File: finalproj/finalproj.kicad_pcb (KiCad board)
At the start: 2 copper layers, 35 parts, among them J10 Motor Out B, J11 Motor Out A, J5 Stepper_Motor_Controller, J7 LIDAR_Connector, J9 RPI_UART_Conn, U2 LM1085-12, U3 LM1085-5.0, U4 LM1085-3.3, U5 L298N

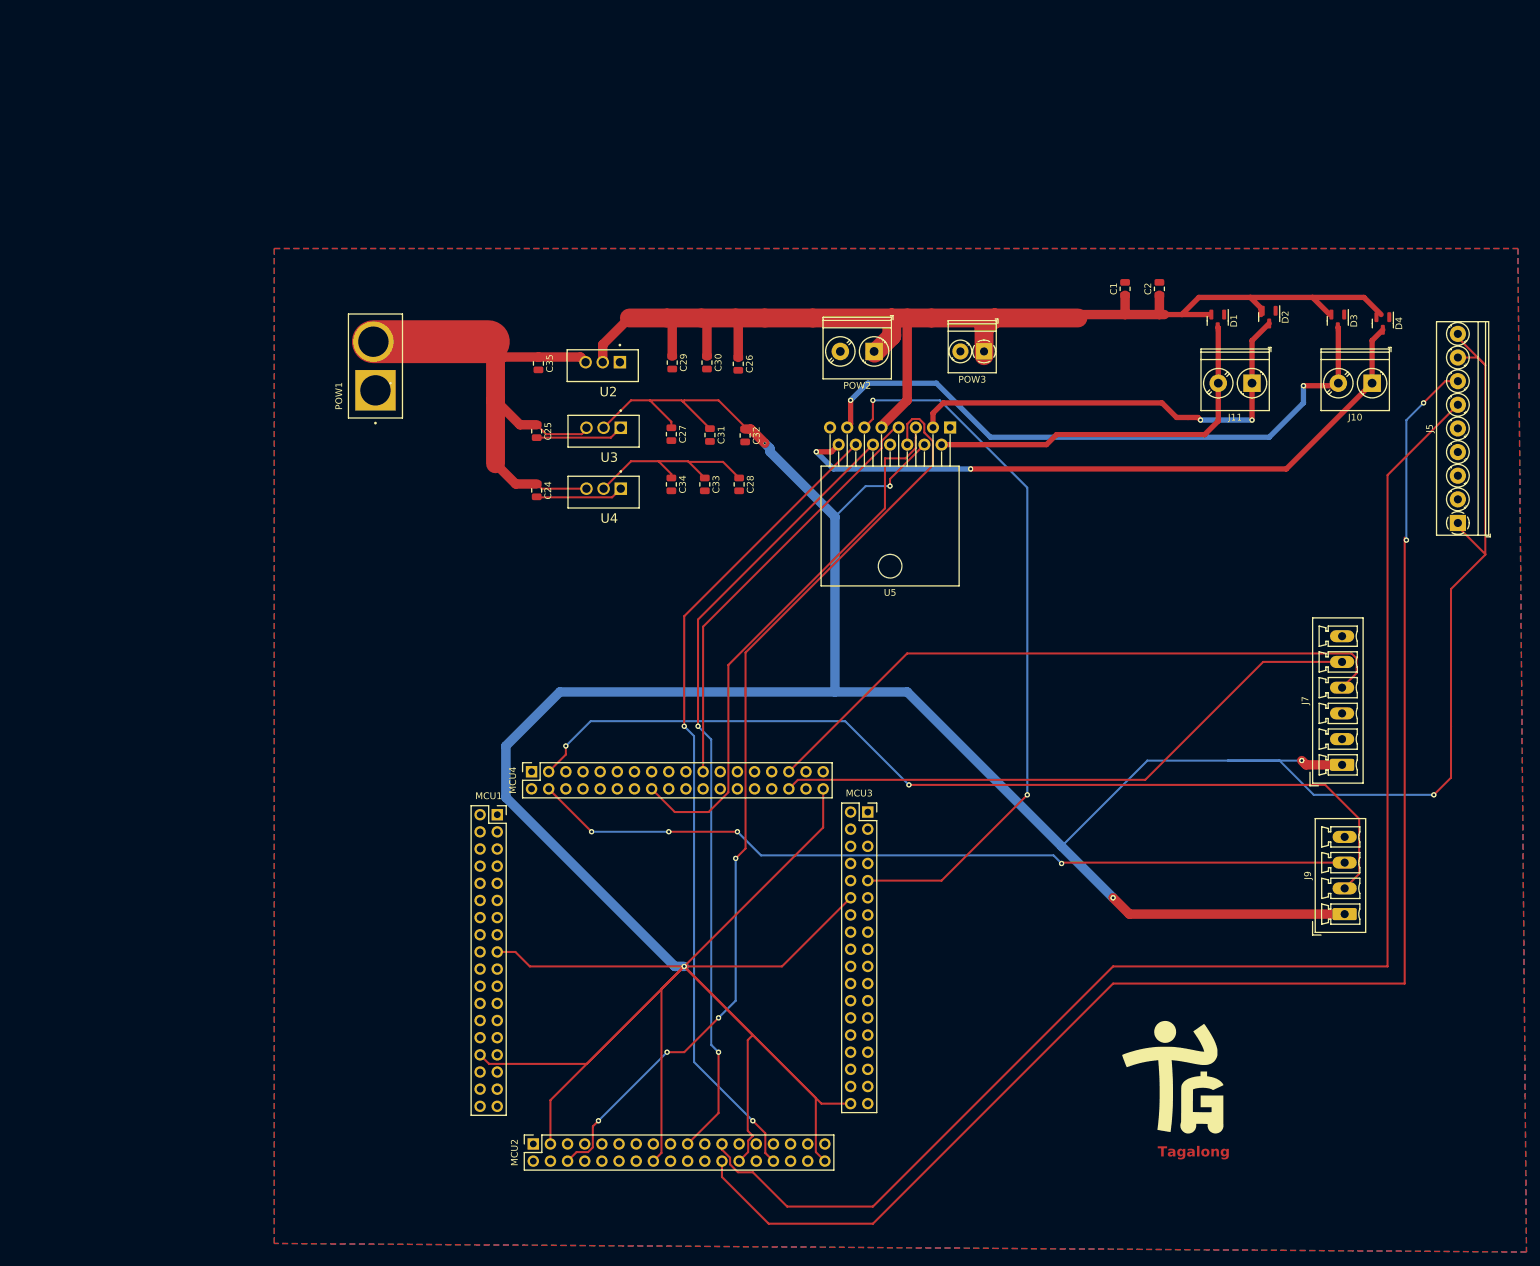
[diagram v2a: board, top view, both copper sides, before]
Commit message: resized the board and fixed errors
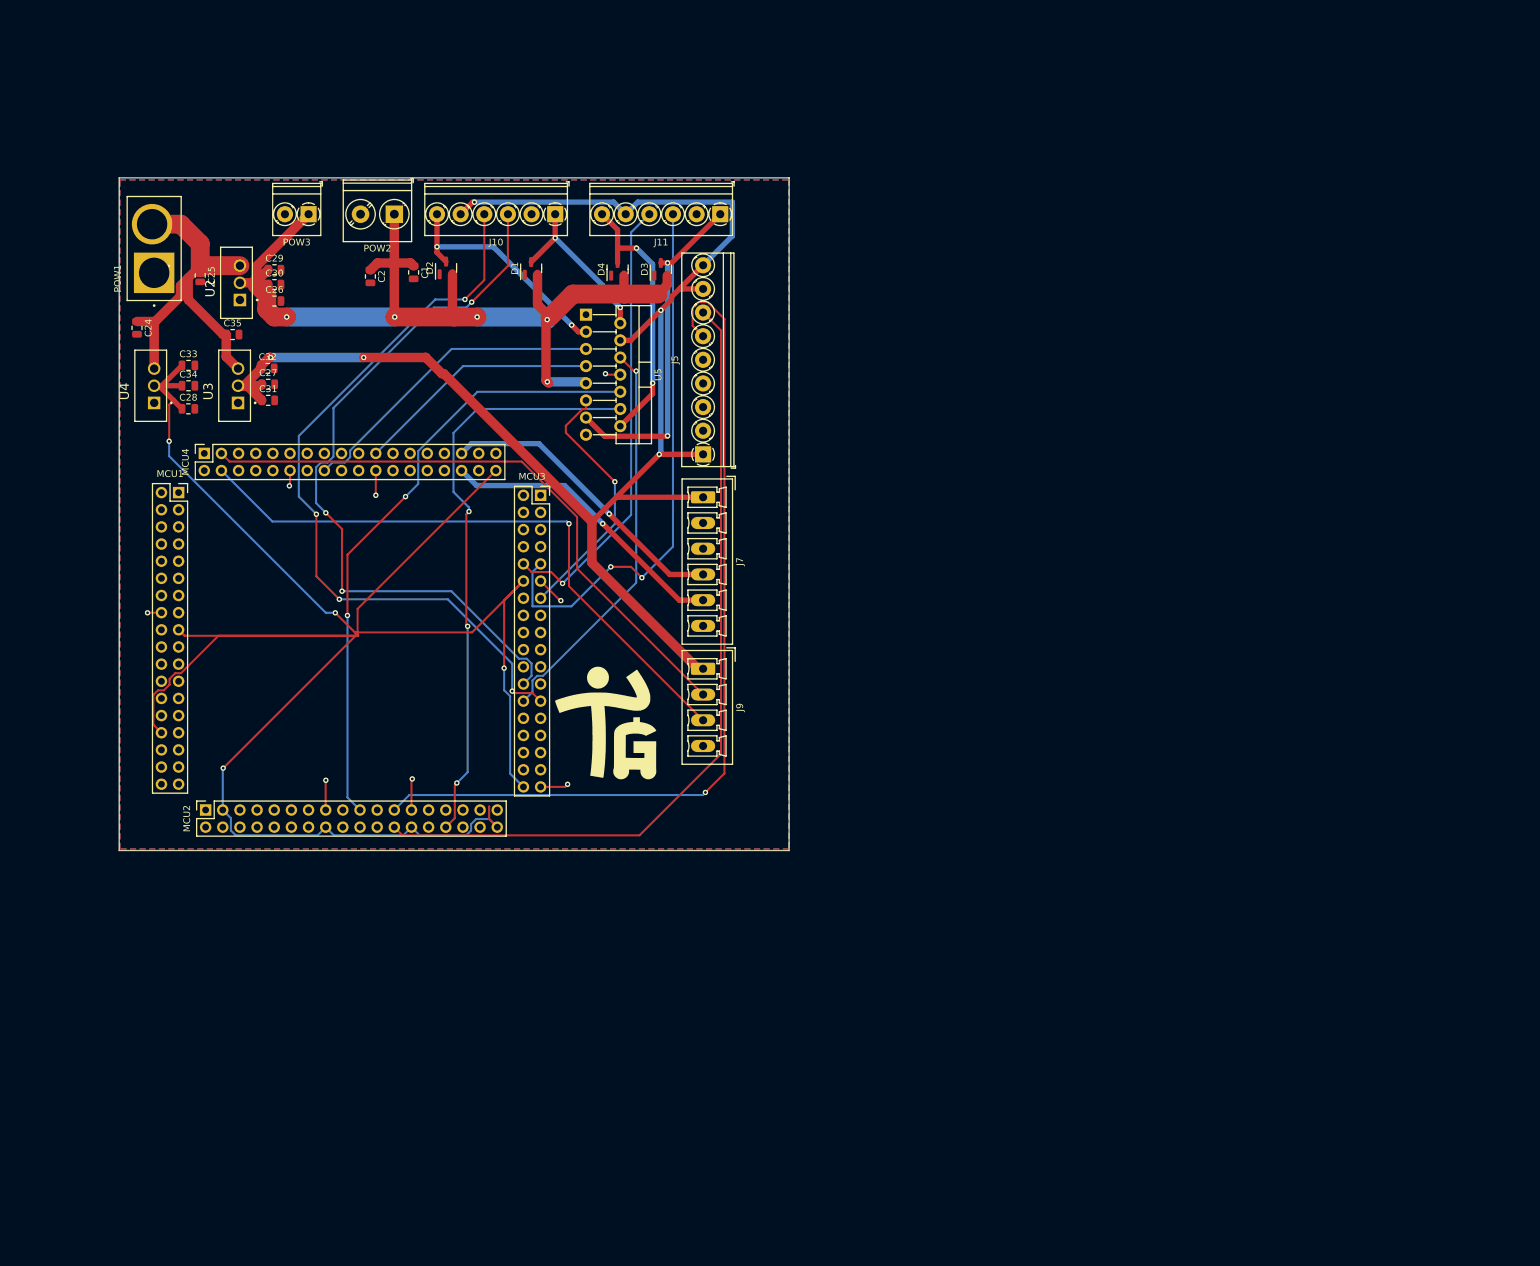
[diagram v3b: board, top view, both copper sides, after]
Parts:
- J10: value Motor Out B -> MotorA Out; footprint TerminalBlock_Phoenix:TerminalBlock_Phoenix_PT-1,5-2-5.0-H_1x02_P5.00mm_Horizontal -> TerminalBlock_Phoenix:TerminalBlock_Phoenix_PT-1,5-6-3.5-H_1x06_P3.50mm_Horizontal
- J11: value Motor Out A -> MotorB Out; footprint TerminalBlock_Phoenix:TerminalBlock_Phoenix_PT-1,5-2-5.0-H_1x02_P5.00mm_Horizontal -> TerminalBlock_Phoenix:TerminalBlock_Phoenix_PT-1,5-6-3.5-H_1x06_P3.50mm_Horizontal
- U5: footprint Package_TO_SOT_THT:TO-220-15_P2.54x2.54mm_StaggerOdd_Lead5.84mm_TabDown -> Package_TO_SOT_THT:TO-220-15_P2.54x2.54mm_StaggerOdd_Lead4.58mm_Vertical
- moved J10 123.5 mm to (77.2, 17.8)
- moved D2 122.1 mm to (61.0, 25.7), turned to 90 degrees
- moved C2 116.8 mm to (49.8, 27.0), turned to -90 degrees
- moved D4 113.6 mm to (86.4, 25.9), turned to 90 degrees
- moved J5 112.2 mm to (99.1, 53.3)
- moved C1 105.4 mm to (56.2, 26.4), turned to -90 degrees
- moved J7 102.6 mm to (99.1, 59.7), turned to -90 degrees
- moved POW3 102.1 mm to (40.6, 17.8)
- moved D1 102.0 mm to (73.6, 25.8), turned to 90 degrees
- moved J9 101.7 mm to (99.1, 85.1), turned to -90 degrees
- moved D3 100.5 mm to (92.8, 25.9), turned to 90 degrees
- moved G*** 99.0 mm to (86.2, 93.6)
- moved J11 82.6 mm to (101.6, 17.8)
- moved C28 82.3 mm to (22.9, 46.6), turned to 0 degrees
- moved C33 78.5 mm to (22.9, 40.2), turned to 0 degrees
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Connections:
- C27 pad 1: VDD -> +5V
- C28 pad 1: +3.3V -> VDD
- C31 pad 1: VDD -> +5V
- C32 pad 1: VDD -> +5V
- C33 pad 1: +3.3V -> VDD
- C34 pad 1: +3.3V -> VDD
- J10 pad 1: MotorOutB2 -> MotorOutA1
- J10 pad 2: MotorOutB1 -> VSS
- J11 pad 1: MotorOutA2 -> MotorOutB1
- J11 pad 2: MotorOutA1 -> VSS
- J5 pad 1: VDD -> +5V
- J5 pad 8: VDD -> +5V
- J5 pad 9: VDD -> +5V
- J7 pad 1: VDD -> +5V
- J9 pad 1: VDD -> +5V
- MCU2 pad 42: MotorAPWM -> unconnected-(MCU2-PA6-Pad42)
- MCU3 pad 81: MotorBPWM -> EncoderBFeedback1
- MCU3 pad 82: unconnected-(MCU3-PD13-Pad82) -> EncoderBFeedback2
- MCU3 pad 85: unconnected-(MCU3-PD14-Pad85) -> MotorBPWM
- MCU3 pad 96: unconnected-(MCU3-PC6-Pad96) -> EncoderAFeedback1
- MCU3 pad 97: unconnected-(MCU3-PC7-Pad97) -> EncoderAFeedback2
- MCU3 pad 98: unconnected-(MCU3-PC8-Pad98) -> MotorAPWM
- U3 pad 2: VDD -> +5V
- U4 pad 2: +3.3V -> VDD
- U5 pad 4: VDD -> +5V
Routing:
- net VDD: track 746.9 -> 308.5 mm, vias 6 -> 4
- net +5V: track 0.00 -> 232.0 mm, vias 0 -> 5
- net EncoderAFeedback2: track 0.00 -> 111.9 mm, vias 0 -> 4
- net EncoderAFeedback1: track 0.00 -> 108.6 mm, vias 0 -> 3
- net STEP_PWM: track 215.1 -> 120.3 mm, vias 2 -> 0
- net EncoderBFeedback1: track 0.00 -> 81.8 mm, vias 0 -> 2
- net MotorAPWM: track 140.7 -> 59.5 mm, vias 4 -> 1
- net STEP_DIR: track 205.7 -> 129.3 mm, vias 0 -> 1
- net MotorBPWM: track 107.1 -> 38.4 mm, vias 2 -> 1
- net EncoderBFeedback2: track 0.00 -> 67.0 mm, vias 0 -> 1
- net MotorOutB2: track 100.9 -> 40.4 mm
- net LIDAR_SCL: track 96.8 -> 44.4 mm, vias 0 -> 1
- net RPI_UART_TX: track 141.0 -> 90.6 mm, vias 2 -> 0
- net LIDAR_SDA: track 89.7 -> 43.7 mm, vias 0 -> 1
- net MotorOutB1: track 93.9 -> 50.6 mm
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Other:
- board outline added: 99.2 x 99.6 mm
- board text added: "Tagalong PCB v1: March"
- board text removed: "Tagalong"

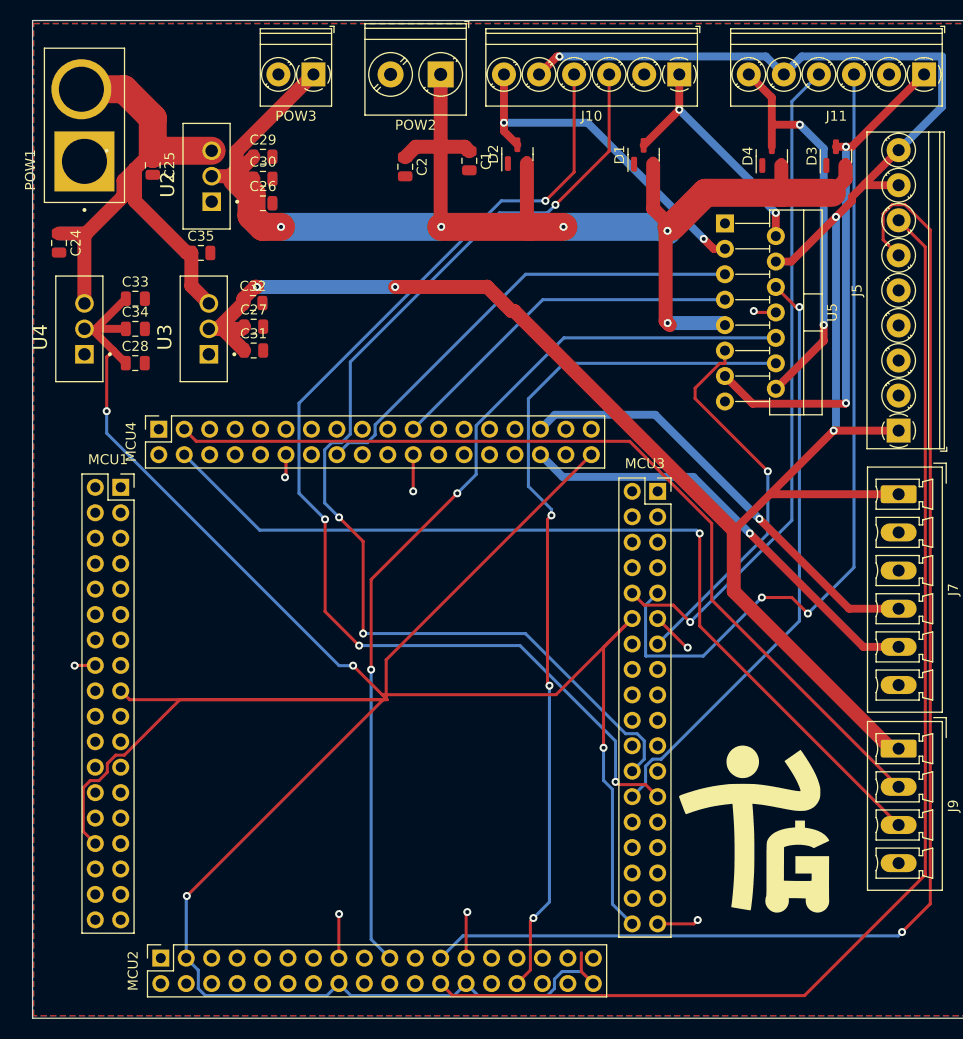
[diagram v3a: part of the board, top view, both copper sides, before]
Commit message: main pcb is completed no warnings
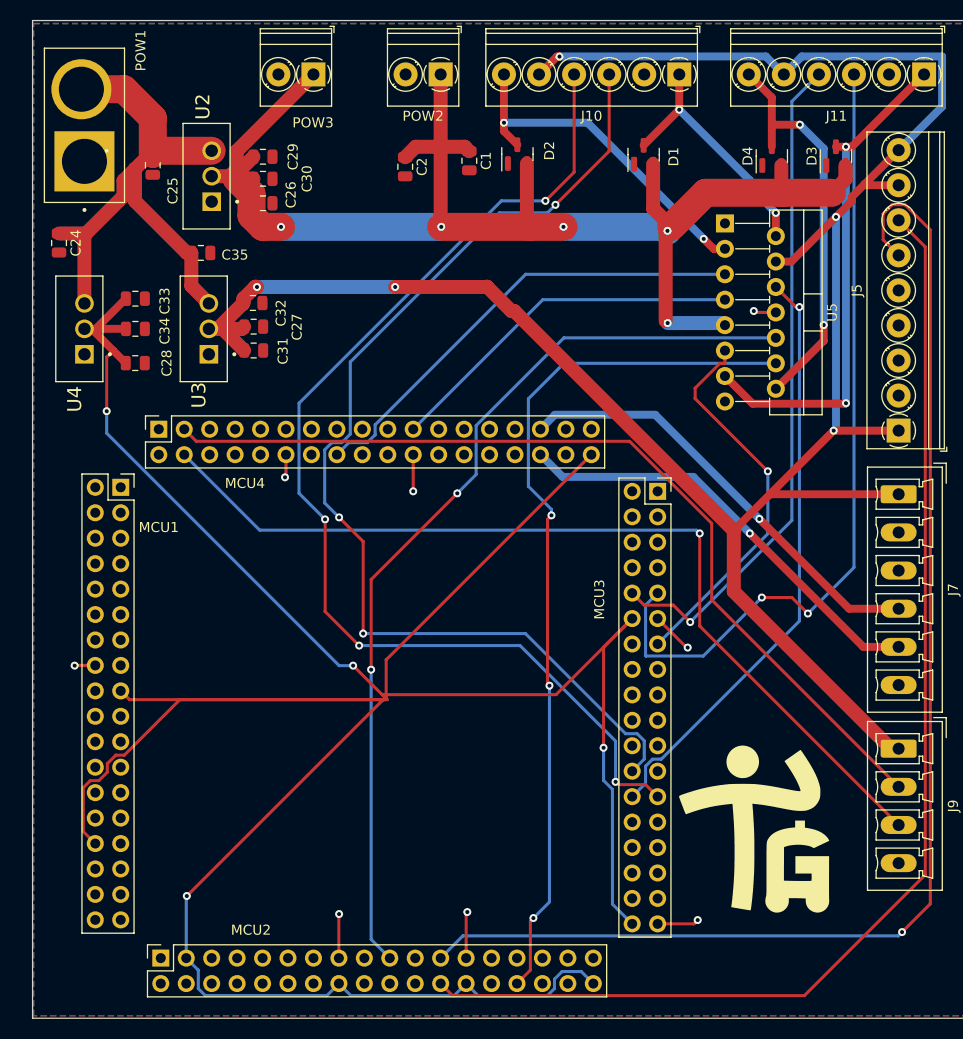
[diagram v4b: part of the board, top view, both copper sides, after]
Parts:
- MCU1: footprint Connector_PinSocket_2.54mm:PinSocket_2x18_P2.54mm_Vertical -> MCU_SOCKETS:MCU1_SOCKET
- MCU2: footprint Connector_PinSocket_2.54mm:PinSocket_2x18_P2.54mm_Vertical -> MCU_SOCKETS:MCU2_SOCKETS
- MCU3: footprint Connector_PinSocket_2.54mm:PinSocket_2x18_P2.54mm_Vertical -> MCU_SOCKETS:MCU3_SOCKETS
- MCU4: footprint Connector_PinSocket_2.54mm:PinSocket_2x18_P2.54mm_Vertical -> MCU_SOCKETS:MCU4_SOCKETS
- POW2: footprint TerminalBlock_Phoenix:TerminalBlock_Phoenix_PT-1,5-2-5.0-H_1x02_P5.00mm_Horizontal -> TerminalBlock_Phoenix:TerminalBlock_Phoenix_PT-1,5-2-3.5-H_1x02_P3.50mm_Horizontal
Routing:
- net VDD: track 308.5 -> 304.4 mm
- net +5V: track 232.0 -> 230.2 mm
- net +12V: track 145.8 -> 145.2 mm

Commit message: finished pcb, pcbway confirmed
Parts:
- added C3: 0.1u, Capacitor_SMD:C_0805_2012Metric, F.Cu at (54.2, 15.4)
- added C4: 0.47u, Capacitor_SMD:C_0805_2012Metric, F.Cu at (44.4, 27.2)
- added C5: 0.1u, Capacitor_SMD:C_0805_2012Metric, F.Cu at (54.2, 17.8)
- added C6: 0.1u, Capacitor_SMD:C_0805_2012Metric, F.Cu at (54.2, 20.6)
- added H1: MountingHole, MountingHole:MountingHole_3.2mm_M3, F.Cu at (27.4, 16.4)
- added H2: MountingHole, MountingHole:MountingHole_3.2mm_M3, F.Cu at (107.8, 16.8)
- added H3: MountingHole, MountingHole:MountingHole_3.2mm_M3, F.Cu at (107.6, 108.2)
- added H4: MountingHole, MountingHole:MountingHole_3.2mm_M3, F.Cu at (15.8, 108.2)
- added U1: LM1085-12, LM1085IT-5.0:TO254P1054X470X1955-3, F.Cu at (52.2, 26.2)
- J7: footprint Connector_Phoenix_MC:PhoenixContact_MCV_1,5_6-G-3.81_1x06_P3.81mm_Vertical -> Connector_PinHeader_2.54mm:PinHeader_1x06_P2.54mm_Vertical
- J9: footprint Connector_Phoenix_MC:PhoenixContact_MCV_1,5_4-G-3.81_1x04_P3.81mm_Vertical -> Connector_PinHeader_2.54mm:PinHeader_1x04_P2.54mm_Vertical
- moved C1 13.1 mm to (61.8, 38.2)
- moved C2 13.0 mm to (56.2, 38.4)
- moved POW2 3.84 mm to (49.5, 17.8)
- moved J9 0.35 mm to (99.4, 85.0), turned to 0 degrees
- turned J7 to 0 degrees
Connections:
- net Net-(POW1-Pin_2) renamed BATTERY_VIN
- MCU4 pad 138: unconnected-(MCU4-BOOT0-Pad138) -> VSS
- POW2 pad 1: +12V -> 12V_IC
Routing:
- net BATTERY_VIN: track 55.1 -> 86.8 mm, vias 0 -> 5
- net 12V_IC: track 0.00 -> 22.9 mm
- net +12V: track 145.2 -> 138.9 mm, vias 5 -> 9
- net +5V: track 230.2 -> 236.0 mm, vias 5 -> 7
- net VSS: track 27.7 -> 31.6 mm, vias 8 -> 9
- net LIDAR_SDA: track 43.7 -> 41.6 mm
- net LIDAR_SCL: track 44.4 -> 42.9 mm
- net RPI_UART_RX: track 92.1 -> 91.3 mm
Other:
- board text added: "TEAM 36: TAGALONG PCB_V1 MARCH"
